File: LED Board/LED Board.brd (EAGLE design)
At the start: 100 x 80 mm, 3 parts

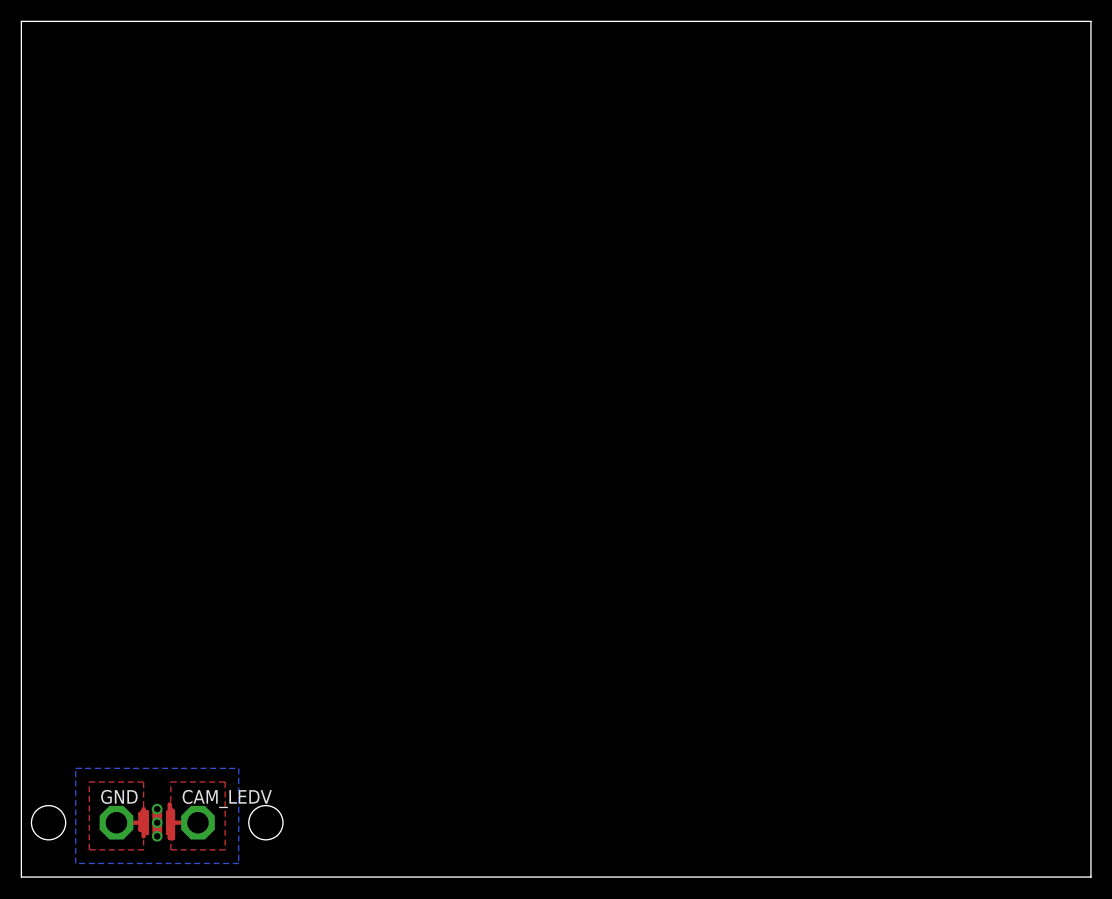
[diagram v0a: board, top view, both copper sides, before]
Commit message: Updated LED board
Ready for manufacturing
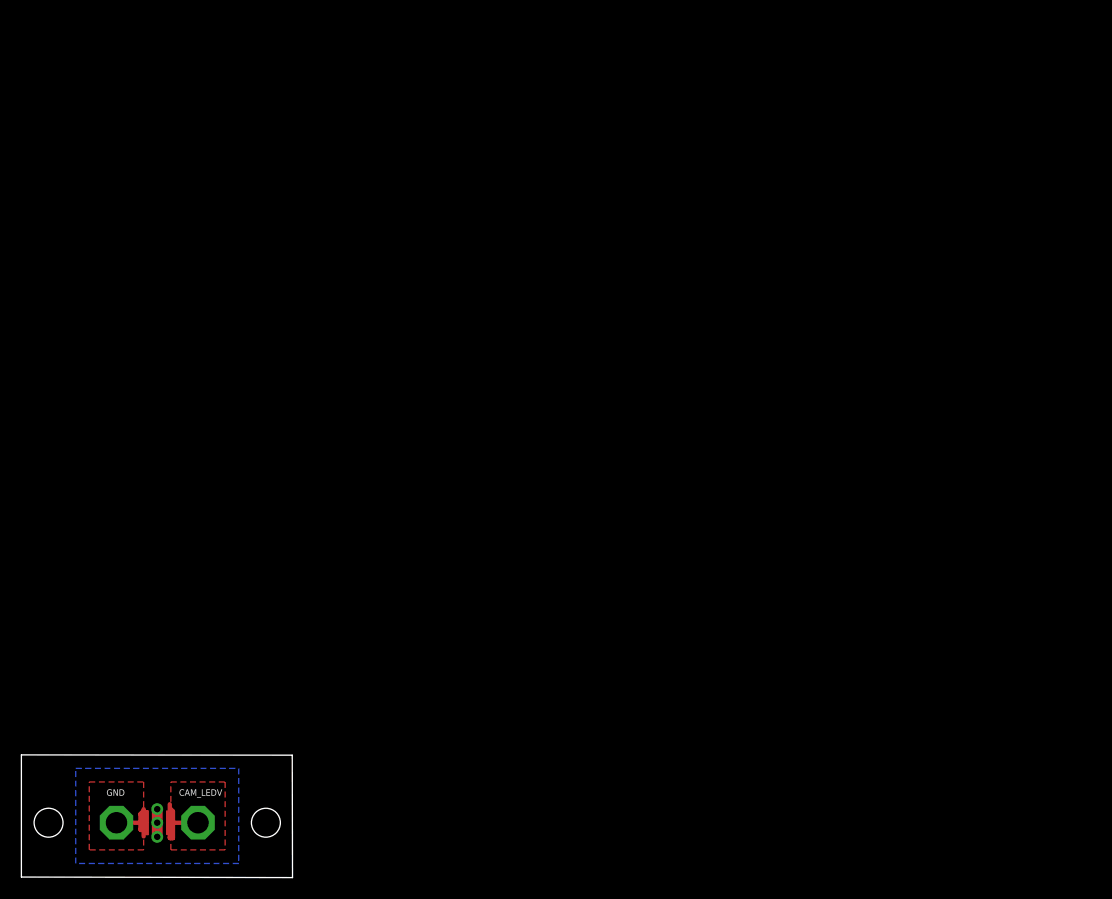
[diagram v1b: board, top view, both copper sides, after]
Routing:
- net GND: track 7.30 -> 10.2 mm
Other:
- board size 100 x 80 mm -> 25.3 x 11.5 mm
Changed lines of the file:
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@@
 <?xml version="1.0" encoding="utf-8"?>
 <!DOCTYPE eagle SYSTEM "eagle.dtd">
-<eagle version="7.4.0">
+<eagle version="7.1.0">
 <drawing>
 <settings>
@@
 <board>
 <plain>
-<wire x1="0" y1="0" x2="100" y2="0" width="0" layer="20"/>
-<wire x1="100" y1="0" x2="100" y2="80" width="0" layer="20"/>
-<wire x1="100" y1="80" x2="0" y2="80" width="0" layer="20"/>
-<wire x1="0" y1="80" x2="0" y2="0" width="0" layer="20"/>
-<hole x="22.86" y="5.08" drill="3.2"/>
-<hole x="2.54" y="5.08" drill="3.2"/>
+<wire x1="0" y1="0" x2="25.3494" y2="-0.0508" width="0" layer="20"/>
+<wire x1="25.3494" y1="-0.0508" x2="25.324" y2="11.3946" width="0" layer="20"/>
+<wire x1="25.324" y1="11.3946" x2="0" y2="11.42" width="0" layer="20"/>
+<wire x1="0" y1="11.42" x2="0" y2="0" width="0" layer="20"/>
+<hole x="22.86" y="5.08" drill="2.7051"/>
+<hole x="2.54" y="5.08" drill="2.7051"/>
 </plain>
 <attributes>
@@
 </class>
 </classes>
-<designrules name="default">
-<description language="de">&lt;b&gt;EAGLE Design Rules&lt;/b&gt;
+<designrules name="GoldPhoenix">
+<description language="en">
+&lt;b&gt;Gold Phoenix PCB Design Rules&lt;/b&gt;
 &lt;p&gt;
-Die Standard-Design-Rules sind so gewählt, dass sie für
-die meisten Anwendungen passen. Sollte ihre Platine
-besondere Anforderungen haben, treffen Sie die erforderlichen
-Einstellungen hier und speichern die Design Rules unter
-einem neuen Namen ab.</description>
-<description language="en">&lt;b&gt;EAGLE Design Rules&lt;/b&gt;
-&lt;p&gt;
-The default Design Rules have been set to cover
-a wide range of applications. Your particular design
-may have different requirements, so please make the
-necessary adjustments and save your customized
-design rules under a new name.</description>
+Created by Nick Molo for the Purdue IEEE ROV Team
+</description>
 <param name="layerSetup" value="(1*16)"/>
 <param name="mtCopper" value="0.035mm 0.035mm 0.035mm 0.035mm 0.035mm 0.035mm 0.035mm 0.035mm 0.035mm 0.035mm 0.035mm 0.035mm 0.035mm 0.035mm 0.035mm 0.035mm"/>
 <param name="mtIsolate" value="1.5mm 0.15mm 0.2mm 0.15mm 0.2mm 0.15mm 0.2mm 0.15mm 0.2mm 0.15mm 0.2mm 0.15mm 0.2mm 0.15mm 0.2mm"/>
-<param name="mdWireWire" value="8mil"/>
-<param name="mdWirePad" value="8mil"/>
-<param name="mdWireVia" value="8mil"/>
-<param name="mdPadPad" value="8mil"/>
-<param name="mdPadVia" value="8mil"/>
-<param name="mdViaVia" value="8mil"/>
-<param name="mdSmdPad" value="8mil"/>
-<param name="mdSmdVia" value="8mil"/>
-<param name="mdSmdSmd" value="8mil"/>
+<param name="mdWireWire" value="7mil"/>
+<param name="mdWirePad" value="7mil"/>
+<param name="mdWireVia" value="7mil"/>
+<param name="mdPadPad" value="7mil"/>
+<param name="mdPadVia" value="7mil"/>
+<param name="mdViaVia" value="7mil"/>
+<param name="mdSmdPad" value="7mil"/>
+<param name="mdSmdVia" value="7mil"/>
+<param name="mdSmdSmd" value="7mil"/>
 <param name="mdViaViaSameLayer" value="8mil"/>
 <param name="mnLayersViaInSmd" value="2"/>
-<param name="mdCopperDimension" value="40mil"/>
+<param name="mdCopperDimension" value="10mil"/>
 <param name="mdDrill" value="8mil"/>
 <param name="mdSmdStop" value="0mil"/>
-<param name="msWidth" value="10mil"/>
-<param name="msDrill" value="24mil"/>
+<param name="msWidth" value="7mil"/>
+<param name="msDrill" value="10mil"/>
 <param name="msMicroVia" value="9.99mm"/>
 <param name="msBlindViaRatio" value="0.5"/>
@@
 <param name="rlMinPadBottom" value="10mil"/>
 <param name="rlMaxPadBottom" value="20mil"/>
-<param name="rlMinViaOuter" value="8mil"/>
+<param name="rlMinViaOuter" value="10mil"/>
 <param name="rlMaxViaOuter" value="20mil"/>
-<param name="rlMinViaInner" value="8mil"/>
+<param name="rlMinViaInner" value="10mil"/>
 <param name="rlMaxViaInner" value="20mil"/>
 <param name="rlMinMicroViaOuter" value="4mil"/>
@@
 <param name="mlMinCreamFrame" value="0mil"/>
 <param name="mlMaxCreamFrame" value="0mil"/>
-<param name="mlViaStopLimit" value="0mil"/>
+<param name="mlViaStopLimit" value="25mil"/>
 <param name="srRoundness" value="0"/>
 <param name="srMinRoundness" value="0mil"/>
@@
 <elements>
 <element name="D1" library="2015_LED_Driver" package="CREE-XLAMP-XM-L" value="CREE" x="12.7" y="5.08"/>
-<element name="CAM_LEDV" library="testpad" package="P1-20" value="PTR1PAD1-20" x="16.51" y="5.08">
-<attribute name="TP_SIGNAL_NAME" value="" x="16.51" y="5.08" size="1.778" layer="27" display="off"/>
+<element name="CAM_LEDV" library="testpad" package="P1-20" value="PTR1PAD1-20" x="16.51" y="5.08" smashed="yes">
+<attribute name="TP_SIGNAL_NAME" value="" x="15.24" y="1.905" size="1" layer="37"/>
+<attribute name="NAME" x="14.732" y="7.5946" size="0.6096" layer="25" ratio="10"/>
+<attribute name="VALUE" x="16.51" y="5.08" size="0.0254" layer="27"/>
 </element>
-<element name="GND" library="testpad" package="P1-20" value="PTR1PAD1-20" x="8.89" y="5.08">
-<attribute name="TP_SIGNAL_NAME" value="" x="8.89" y="5.08" size="1.778" layer="27" display="off"/>
+<element name="GND" library="testpad" package="P1-20" value="PTR1PAD1-20" x="8.89" y="5.08" smashed="yes">
+<attribute name="TP_SIGNAL_NAME" value="" x="7.62" y="1.905" size="1" layer="37"/>
+<attribute name="NAME" x="7.9502" y="7.5946" size="0.6096" layer="25" ratio="10"/>
+<attribute name="VALUE" x="8.89" y="5.08" size="0.0254" layer="27"/>
 </element>
 </elements>
@@
 <via x="12.7" y="5.08" extent="1-16" drill="0.6" diameter="0.0254"/>
 <wire x1="11.7" y1="5.08" x2="11.43" y2="5.08" width="0.3048" layer="1"/>
-<via x="12.7" y="3.81" extent="1-16" drill="0.6" diameter="0.0254"/>
-<wire x1="11.7" y1="5.08" x2="11.715" y2="5.08" width="0" layer="19" extent="1-1"/>
+<via x="12.7" y="3.7592" extent="1-16" drill="0.6" diameter="0.0254"/>
+<wire x1="11.715" y1="5.08" x2="11.43" y2="5.08" width="0.4064" layer="1"/>
+<wire x1="12.7" y1="5.08" x2="12.7" y2="6.35" width="1.016" layer="1"/>
+<wire x1="12.7" y1="3.7592" x2="12.7" y2="5.08" width="1.016" layer="1"/>
 </signal>
 <signal name="CAM_LEDV">

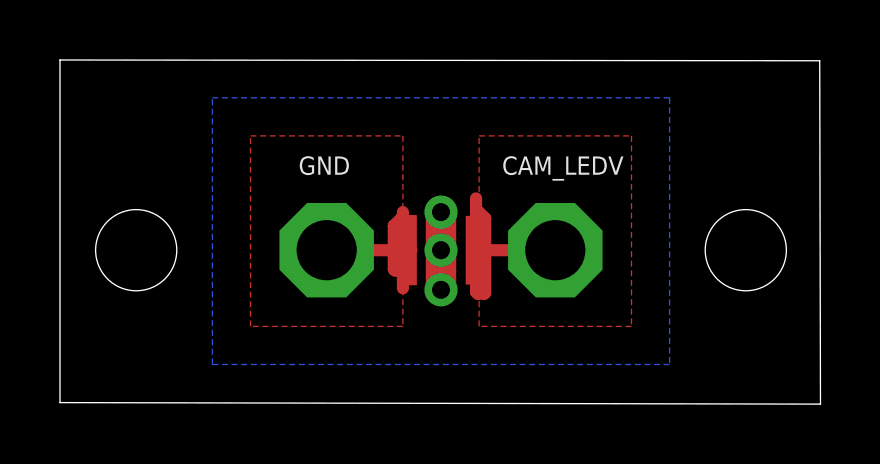
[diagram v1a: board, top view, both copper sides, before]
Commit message: Added symbols to the LED board
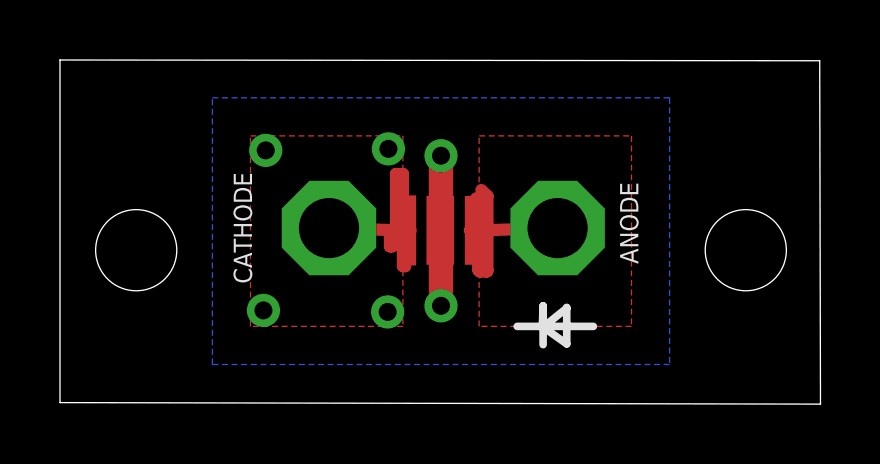
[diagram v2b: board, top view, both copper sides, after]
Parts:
- removed CAM_LEDV, GND: PTR1PAD1-20, testpad:P1-20
- added ANODE, CATHODE: PTR1PAD1-20, testpad:P1-20
- moved D1 0.66 mm to (12.7, 5.74)
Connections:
- net CAM_LEDV: now also ANODE.TP; no longer CAM_LEDV.TP
- net GND: now also CATHODE.TP; no longer GND.TP
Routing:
- net GND: track 10.2 -> 15.9 mm, vias 3 -> 2
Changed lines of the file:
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@@
 <?xml version="1.0" encoding="utf-8"?>
 <!DOCTYPE eagle SYSTEM "eagle.dtd">
-<eagle version="7.1.0">
+<eagle version="7.5.0">
 <drawing>
 <settings>
@@
 <hole x="22.86" y="5.08" drill="2.7051"/>
 <hole x="2.54" y="5.08" drill="2.7051"/>
+<wire x1="17.78" y1="8.8392" x2="16.0782" y2="8.8392" width="0.254" layer="22"/>
+<wire x1="16.0782" y1="8.8392" x2="15.24" y2="8.8392" width="0.254" layer="22"/>
+<wire x1="16.891" y1="8.255" x2="16.891" y2="9.4488" width="0.254" layer="22"/>
+<wire x1="16.891" y1="9.4488" x2="16.891" y2="9.4742" width="0.254" layer="22"/>
+<wire x1="16.891" y1="8.255" x2="16.1036" y2="8.8138" width="0.254" layer="22"/>
+<wire x1="16.1036" y1="8.8138" x2="16.891" y2="9.4488" width="0.254" layer="22"/>
+<wire x1="16.0782" y1="8.8392" x2="16.1036" y2="9.525" width="0.254" layer="22"/>
+<wire x1="16.1036" y1="9.525" x2="16.1036" y2="8.2296" width="0.254" layer="22"/>
+<wire x1="17.78" y1="2.54" x2="16.0782" y2="2.54" width="0.254" layer="21"/>
+<wire x1="16.0782" y1="2.54" x2="15.24" y2="2.54" width="0.254" layer="21"/>
+<wire x1="16.891" y1="1.9558" x2="16.891" y2="3.1496" width="0.254" layer="21"/>
+<wire x1="16.891" y1="3.1496" x2="16.891" y2="3.175" width="0.254" layer="21"/>
+<wire x1="16.891" y1="1.9558" x2="16.1036" y2="2.5146" width="0.254" layer="21"/>
+<wire x1="16.1036" y1="2.5146" x2="16.891" y2="3.1496" width="0.254" layer="21"/>
+<wire x1="16.0782" y1="2.54" x2="16.1036" y2="3.2258" width="0.254" layer="21"/>
+<wire x1="16.1036" y1="3.2258" x2="16.1036" y2="1.9304" width="0.254" layer="21"/>
 </plain>
 <attributes>
@@
 </autorouter>
 <elements>
-<element name="D1" library="2015_LED_Driver" package="CREE-XLAMP-XM-L" value="CREE" x="12.7" y="5.08"/>
-<element name="CAM_LEDV" library="testpad" package="P1-20" value="PTR1PAD1-20" x="16.51" y="5.08" smashed="yes">
-<attribute name="TP_SIGNAL_NAME" value="" x="15.24" y="1.905" size="1" layer="37"/>
-<attribute name="NAME" x="14.732" y="7.5946" size="0.6096" layer="25" ratio="10"/>
-<attribute name="VALUE" x="16.51" y="5.08" size="0.0254" layer="27"/>
+<element name="D1" library="2015_LED_Driver" package="CREE-XLAMP-XM-L" value="CREE" x="12.6746" y="5.7404"/>
+<element name="ANODE" library="testpad" package="P1-20" value="PTR1PAD1-20" x="16.5862" y="5.8166" smashed="yes">
+<attribute name="TP_SIGNAL_NAME" value="" x="15.3162" y="2.6416" size="1" layer="37"/>
+<attribute name="NAME" x="19.2786" y="4.6228" size="0.6096" layer="25" ratio="10" rot="R90"/>
+<attribute name="VALUE" x="16.5862" y="5.8166" size="0.0254" layer="27"/>
 </element>
-<element name="GND" library="testpad" package="P1-20" value="PTR1PAD1-20" x="8.89" y="5.08" smashed="yes">
-<attribute name="TP_SIGNAL_NAME" value="" x="7.62" y="1.905" size="1" layer="37"/>
-<attribute name="NAME" x="7.9502" y="7.5946" size="0.6096" layer="25" ratio="10"/>
-<attribute name="VALUE" x="8.89" y="5.08" size="0.0254" layer="27"/>
+<element name="CATHODE" library="testpad" package="P1-20" value="PTR1PAD1-20" x="8.9662" y="5.8166" smashed="yes">
+<attribute name="TP_SIGNAL_NAME" value="" x="7.6962" y="2.6416" size="1" layer="37"/>
+<attribute name="NAME" x="6.4008" y="3.9624" size="0.6096" layer="25" ratio="10" rot="R90"/>
+<attribute name="VALUE" x="8.9662" y="5.8166" size="0.0254" layer="27"/>
 </element>
 </elements>
@@
 <contactref element="D1" pad="C"/>
 <contactref element="D1" pad="C1"/>
-<contactref element="GND" pad="TP"/>
-<wire x1="8.89" y1="5.08" x2="11.43" y2="5.08" width="0.4064" layer="1"/>
-<wire x1="11.43" y1="5.08" x2="11.43" y2="6.1976" width="0.4064" layer="1"/>
-<wire x1="11.43" y1="3.81" x2="11.43" y2="5.08" width="0.4064" layer="1"/>
-<wire x1="11.43" y1="6.35" x2="11.43" y2="6.1976" width="0.4064" layer="1"/>
-<wire x1="11.43" y1="6.1976" x2="11.1252" y2="5.8928" width="0.4064" layer="1"/>
-<wire x1="11.1252" y1="5.8928" x2="11.1252" y2="4.445" width="0.4064" layer="1"/>
-<wire x1="11.1252" y1="4.445" x2="11.176" y2="4.3942" width="0.4064" layer="1"/>
-<via x="12.7" y="6.35" extent="1-16" drill="0.6" diameter="0.0254"/>
-<via x="12.7" y="5.08" extent="1-16" drill="0.6" diameter="0.0254"/>
-<wire x1="11.7" y1="5.08" x2="11.43" y2="5.08" width="0.3048" layer="1"/>
-<via x="12.7" y="3.7592" extent="1-16" drill="0.6" diameter="0.0254"/>
-<wire x1="11.715" y1="5.08" x2="11.43" y2="5.08" width="0.4064" layer="1"/>
-<wire x1="12.7" y1="5.08" x2="12.7" y2="6.35" width="1.016" layer="1"/>
-<wire x1="12.7" y1="3.7592" x2="12.7" y2="5.08" width="1.016" layer="1"/>
+<contactref element="CATHODE" pad="TP"/>
+<wire x1="8.9662" y1="5.8166" x2="11.4046" y2="5.7404" width="0.4064" layer="1"/>
+<wire x1="11.5062" y1="4.5466" x2="11.4046" y2="5.7404" width="0.4064" layer="1"/>
+<wire x1="11.6746" y1="5.7404" x2="11.4046" y2="5.7404" width="0.3048" layer="1"/>
+<wire x1="11.6896" y1="5.7404" x2="11.4046" y2="5.7404" width="0.4064" layer="1"/>
+<wire x1="11.5062" y1="4.5466" x2="11.43" y2="4.5466" width="0.4064" layer="1"/>
+<wire x1="11.43" y1="4.5466" x2="11.43" y2="5.461" width="0.4064" layer="1"/>
+<wire x1="11.43" y1="5.461" x2="11.43" y2="7.62" width="0.4064" layer="1"/>
+<wire x1="11.43" y1="7.62" x2="11.2014" y2="7.62" width="0.4064" layer="1"/>
+<wire x1="11.2014" y1="7.62" x2="11.2014" y2="5.6896" width="0.4064" layer="1"/>
+<wire x1="11.2014" y1="5.6896" x2="11.0744" y2="5.6896" width="0.4064" layer="1"/>
+<wire x1="11.0744" y1="5.6896" x2="11.0744" y2="5.207" width="0.4064" layer="1"/>
+<wire x1="11.0744" y1="5.207" x2="10.9982" y2="5.207" width="0.4064" layer="1"/>
+<wire x1="10.9982" y1="5.207" x2="10.9982" y2="5.461" width="0.4064" layer="1"/>
+<wire x1="10.9982" y1="5.461" x2="11.43" y2="5.461" width="0.4064" layer="1"/>
+<polygon width="0.4064" layer="1">
+<vertex x="12.9032" y="5.461"/>
+<vertex x="12.9286" y="5.461"/>
+<vertex x="12.9032" y="5.3594"/>
+</polygon>
+<via x="12.7" y="8.2296" extent="1-16" drill="0.6"/>
+<via x="12.7" y="3.2258" extent="1-16" drill="0.6"/>
+<wire x1="12.7" y1="3.2258" x2="12.7" y2="8.2042" width="0.8128" layer="1"/>
 </signal>
 <signal name="CAM_LEDV">
@@
 <contactref element="D1" pad="A@1"/>
 <contactref element="D1" pad="A"/>
-<contactref element="CAM_LEDV" pad="TP"/>
-<wire x1="16.51" y1="5.08" x2="13.97" y2="5.08" width="0.4064" layer="1"/>
-<wire x1="13.8684" y1="6.8072" x2="13.8684" y2="3.683" width="0.4064" layer="1"/>
-<wire x1="13.8684" y1="3.683" x2="13.9192" y2="3.6322" width="0.4064" layer="1"/>
-<wire x1="13.9192" y1="3.6322" x2="14.1478" y2="3.6322" width="0.4064" layer="1"/>
-<wire x1="14.1478" y1="3.6322" x2="14.1732" y2="3.6576" width="0.4064" layer="1"/>
-<wire x1="14.1732" y1="3.6576" x2="14.1732" y2="6.1468" width="0.4064" layer="1"/>
-<wire x1="14.1732" y1="6.1468" x2="13.97" y2="6.35" width="0.4064" layer="1"/>
-<wire x1="14.1732" y1="6.1468" x2="13.97" y2="6.1468" width="0.3048" layer="1"/>
-<wire x1="13.97" y1="6.1468" x2="13.97" y2="6.35" width="0.3048" layer="1"/>
-<wire x1="13.97" y1="6.1468" x2="13.97" y2="5.08" width="0.3048" layer="1"/>
-<wire x1="13.97" y1="5.08" x2="13.685" y2="5.08" width="0" layer="19" extent="1-1"/>
+<contactref element="ANODE" pad="TP"/>
+<wire x1="16.5862" y1="5.8166" x2="13.9446" y2="5.7404" width="0.4064" layer="1"/>
+<wire x1="13.8684" y1="6.8072" x2="13.9446" y2="4.4196" width="0.4064" layer="1"/>
+<wire x1="13.9446" y1="4.4196" x2="13.9954" y2="4.3688" width="0.4064" layer="1"/>
+<wire x1="13.9954" y1="4.3688" x2="14.224" y2="4.3688" width="0.4064" layer="1"/>
+<wire x1="14.224" y1="4.3688" x2="14.2494" y2="4.3942" width="0.4064" layer="1"/>
+<wire x1="14.2494" y1="4.3942" x2="14.2494" y2="6.8834" width="0.4064" layer="1"/>
+<wire x1="14.2494" y1="6.8834" x2="14.0462" y2="7.0866" width="0.4064" layer="1"/>
+<wire x1="14.2494" y1="6.8834" x2="14.0462" y2="6.8834" width="0.3048" layer="1"/>
+<wire x1="14.0462" y1="6.8834" x2="14.0462" y2="7.0866" width="0.3048" layer="1"/>
+<wire x1="14.0462" y1="6.8834" x2="13.9985625" y2="6.3474625" width="0.3048" layer="1"/>
+<wire x1="13.9985625" y1="6.3474625" x2="13.9446" y2="5.7404" width="0.3048" layer="1"/>
+<wire x1="13.6596" y1="5.7404" x2="13.9985625" y2="5.7404" width="0.4064" layer="1"/>
+<wire x1="13.9985625" y1="5.7404" x2="13.9985625" y2="6.3474625" width="0.4064" layer="1"/>
+</signal>
+<signal name="N$1">
+<via x="6.858" y="8.4074" extent="1-16" drill="0.6"/>
+</signal>
+<signal name="N$2">
+<via x="10.9474" y="8.4582" extent="1-16" drill="0.6"/>
+</signal>
+<signal name="N$3">
+<via x="6.7818" y="3.0734" extent="1-16" drill="0.6"/>
+</signal>
+<signal name="N$4">
+<via x="10.922" y="3.0226" extent="1-16" drill="0.6"/>
 </signal>
 </signals>
